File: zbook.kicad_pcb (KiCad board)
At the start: 4 copper layers, 189 parts, among them J1 USB_C_Receptacle_USB2.0_16P, J2 B2B-XH-A, J3 USB_C_Receptacle_USB2.0_16P, J4 Conn_01x03_Pin, J5 Conn_01x05_Pin, J6 Conn_02x04_Odd_Even, J7 Conn_02x15_Counter_Clockwise, J8 MSD-4-A, J9 DISPLAY CONN, Q1 Q_NMOS_GSD, Q2 Q_Photo_NPN, Q3 SL2301S, Q4 T2N7002AK,LM, SW1 SW_SPDT, SW2 SW_Push, SW3 SW_Push, SW4 SW_Push, SW5 SW_Push, SW6 SW_Push, SW7 SW_Push, U3 RP2040, U5 W25Q16JVSS, U6 W25Q16JVSS, U7 GSDA213, Y1 12MHz/10pF, Y2 12MHz/10pF

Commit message: wip: placement
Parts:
- added Q5: T2N7002AK,LM, Package_TO_SOT_SMD:SOT-23, F.Cu at (134.3, 97.3)
- added R56: 10k, Resistor_SMD:R_0402_1005Metric, F.Cu at (136.8, 97.3)
- J4: value Conn_01x03_Pin -> Conn_01x05_Pin; footprint Connector_PinHeader_2.54mm:PinHeader_1x03_P2.54mm_Vertical -> microcontroller:PogoPins
- moved FID1 357.5 mm to (59.6, 75.2)
- moved FID3 353.9 mm to (62.8, 88.2)
- moved H1 350.8 mm to (61.2, 81.2)
- moved H3 349.3 mm to (64.4, 75.6)
- moved FID4 348.8 mm to (68.8, 79.1)
- moved FID2 344.2 mm to (72.8, 81.0)
- moved H2 344.1 mm to (68.0, 86.4)
- moved H4 340.7 mm to (73.9, 75.8)
- moved R24 333.1 mm to (75.3, 83.2)
- moved R55 323.7 mm to (81.5, 136.0), turned to 180 degrees
- moved R54 323.0 mm to (81.5, 132.7), turned to 180 degrees
- moved D8 321.8 mm to (69.3, 71.2)
- moved J6 318.1 mm to (84.7, 138.0), turned to 180 degrees
- moved C47 315.2 mm to (45.3, 77.3)
- moved C48 315.2 mm to (45.3, 79.3)
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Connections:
- BZ1 pad 1: Net-(BZ1-+) -> +3V3
- BZ1 pad 2: GND -> Net-(BZ1--)
- J4 pad 1: /Microcontroller/SWDIO_RP2040 -> +3V3
- J4 pad 3: GND -> /Microcontroller/SWDIO_RP2040
- J5 pad 1: /Microcontroller/RP2350_TX/BT_WIFI_RX -> /Microcontroller/RP2350_TX/BT_RX
- J5 pad 2: /Microcontroller/RP2350_RX/BT_WIFI_TX -> /Microcontroller/RP2350_RX/BT_TX
- J6 pad 2: /Microcontroller/RP2350_RX/BT_WIFI_TX -> /Microcontroller/RP2350_RX/BT_TX
- J6 pad 7: /Microcontroller/RP2350_TX/BT_WIFI_RX -> /Microcontroller/RP2350_TX/BT_RX
- J7 pad 1: /Microcontroller/GPIO06 -> /Microcontroller/GPIO07
- J7 pad 10: MOSFET_DRAIN -> I2C_SDA
- J7 pad 11: I2C_SDA -> I2C_SCL
- J7 pad 12: I2C_SCL -> SPI_MISO
- J7 pad 13: SPI_MISO -> SPI_SCLK
- J7 pad 14: SPI_SCLK -> SPI_MOSI
- J7 pad 15: SPI_MOSI -> /Microcontroller/RUN_RP2350
- J7 pad 2: /Microcontroller/GPIO07 -> /Microcontroller/GPIO08
- J7 pad 3: /Microcontroller/GPIO08 -> /Microcontroller/GPIO26
- J7 pad 4: /Microcontroller/GPIO26 -> /Microcontroller/GPIO27
- J7 pad 5: /Microcontroller/GPIO27 -> /Microcontroller/GPIO47
- J7 pad 6: /Microcontroller/GPIO47 -> /Microcontroller/GPIO46
- J7 pad 7: /Microcontroller/GPIO46 -> /Microcontroller/GPIO45
- J7 pad 9: /Microcontroller/GPIO45 -> MOSFET_DRAIN
- R35 pad 1: BUZZER_GPIO -> Net-(BZ1--)
- R35 pad 2: Net-(BZ1-+) -> +3V3
- U4 pad 3: /Microcontroller/GPIO06 -> LED_ADDR_GPIO
- U4 pad 9: DISPLAY_RST -> ~{DISPLAY_RST}
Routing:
- net /Power Supply/LDO_EN: track 0.00 -> 1.62 mm
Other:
- board text added: "+3V3"
- board text added: "+5V"
- board text added: "+VBQ"
- board text added: "B"
- board text added: "G"
- board text added: "IR"
- board text added: "R"
- board text added: "Y"

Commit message: feat: finishes first iteration of placement
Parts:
- moved C48 128.3 mm to (166.8, 120.4), turned to -90 degrees
- moved C47 128.1 mm to (165.9, 120.4), turned to -90 degrees
- moved R48 122.7 mm to (167.0, 117.2), turned to 90 degrees
- moved FID1 119.0 mm to (156.2, 144.6)
- moved H1 111.5 mm to (171.7, 66.6)
- moved H3 110.8 mm to (155.7, 138.3)
- moved FID3 108.8 mm to (170.2, 70.8)
- moved FID4 101.3 mm to (167.5, 101.8)
- moved TP13 100.2 mm to (134.5, 108.9)
- moved C50 97.8 mm to (138.9, 111.3), turned to 90 degrees
- moved C49 93.8 mm to (134.2, 111.3), turned to 90 degrees
- moved U7 92.1 mm to (136.6, 111.5)
- moved R46 89.9 mm to (133.8, 98.6), turned to 90 degrees
- moved R47 87.5 mm to (133.8, 100.4), turned to -90 degrees
- moved TP16 81.5 mm to (118.6, 105.5)
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
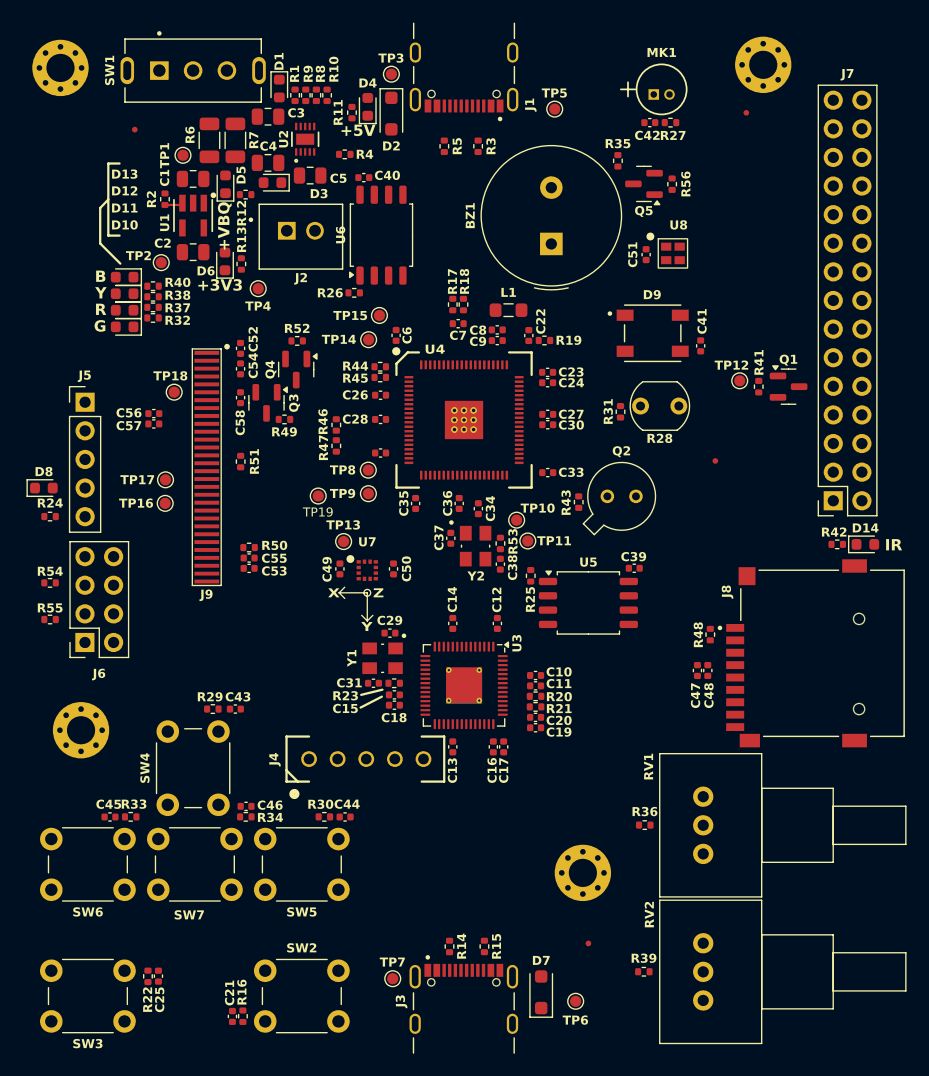
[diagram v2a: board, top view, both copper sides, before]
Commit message: feat: adds GND planes to L2 and L3
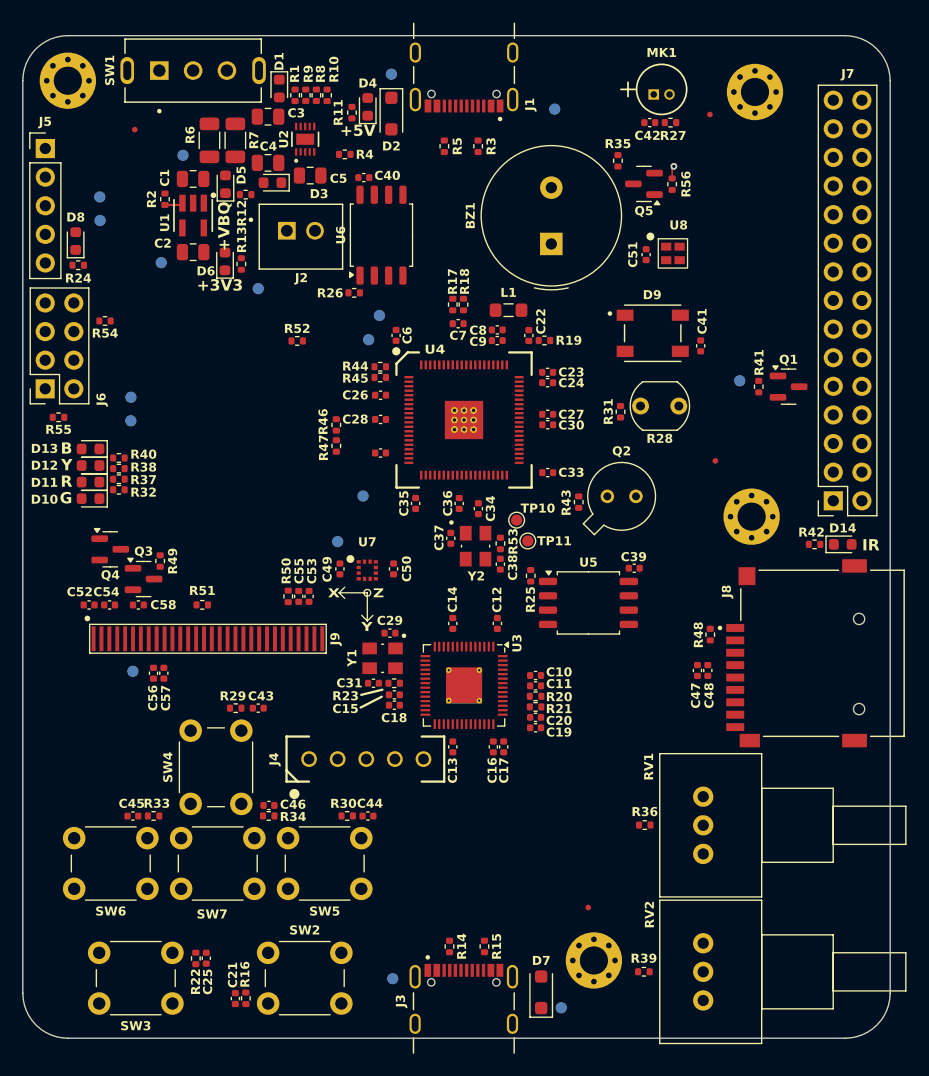
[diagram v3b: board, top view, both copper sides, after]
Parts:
- TP1, TP12, TP13, TP14, TP15, TP16, TP17, TP18, TP19, TP2, TP3, TP4, TP5, TP6, TP7, TP8, TP9: moved to B.Cu
- moved H2 62.5 mm to (170.7, 106.7)
- moved C52 26.5 mm to (111.9, 114.5), turned to 0 degrees
- moved TP17 25.8 mm to (112.8, 78.3), turned to 180 degrees
- moved TP16 25.8 mm to (112.9, 80.4), turned to 180 degrees
- moved TP18 25.0 mm to (115.8, 120.4), turned to -90 degrees
- moved C54 24.0 mm to (113.7, 114.5), turned to 0 degrees
- moved R54 23.8 mm to (113.3, 89.3), turned to 0 degrees
- moved C56 23.1 mm to (117.6, 120.6), turned to -90 degrees
- moved Q4 23.0 mm to (113.8, 109.6), turned to 0 degrees
- moved J5 22.8 mm to (108.0, 74.0)
- moved J6 22.8 mm to (108.0, 95.3)
- moved R24 22.4 mm to (110.9, 84.4), turned to 180 degrees
- moved C57 22.1 mm to (118.5, 120.6), turned to -90 degrees
- moved D8 22.1 mm to (110.7, 82.2), turned to 90 degrees
- moved TP9 22.1 mm to (115.6, 98.2), turned to 180 degrees
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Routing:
- net GND: track 0.00 -> 1.14 mm, vias 0 -> 1
- added copper zone on In1.Cu, net GND
- added copper zone on In2.Cu, net GND
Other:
- board outline added: 77 x 89 mm

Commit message: feat: starts routing
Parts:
- TP10, TP11: moved to B.Cu
- moved Q2 36.4 mm to (154.7, 68.6)
- moved R43 36.4 mm to (152.1, 69.1)
- moved J6 33.7 mm to (108.1, 129.0)
- moved R54 33.7 mm to (113.4, 123.0)
- moved R55 33.7 mm to (109.3, 131.5)
- moved TP16 29.5 mm to (132.8, 102.2)
- moved TP17 29.0 mm to (131.5, 100.5)
- moved R52 26.6 mm to (111.2, 109.6), turned to -90 degrees
- moved D10 25.9 mm to (115.1, 79.4), turned to 90 degrees
- moved D11 24.2 mm to (112.2, 79.4), turned to 90 degrees
- moved TP19 23.5 mm to (112.8, 106.6)
- moved D12 22.8 mm to (113.7, 79.4), turned to 90 degrees
- moved R32 22.4 mm to (114.9, 81.9), turned to 90 degrees
- moved D13 21.8 mm to (116.6, 79.4), turned to 90 degrees
- moved R37 21.5 mm to (113.0, 81.9), turned to 90 degrees
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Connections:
- C10 pad 1: +1V1 -> +1V1_PROBE
- C18 pad 1: +1V1 -> +1V1_PROBE
- C20 pad 2: +1V1 -> +1V1_PROBE
- U3 pad 23: +1V1 -> +1V1_PROBE
- U3 pad 45: +1V1 -> +1V1_PROBE
- U3 pad 50: +1V1 -> +1V1_PROBE
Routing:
- net +3V3: track 0.00 -> 160.8 mm, vias 0 -> 45
- net GND: track 1.14 -> 106.0 mm, vias 1 -> 123
- net /Microcontroller/RUN_RP2350: track 0.00 -> 72.0 mm, vias 0 -> 3
- net /Microcontroller/RUN_RP2040: track 0.00 -> 47.1 mm
- net SPI_SCLK: track 0.00 -> 43.9 mm, vias 0 -> 5
- net +VBUS: track 0.00 -> 43.9 mm, vias 0 -> 4
- net SD_DAT1: track 0.00 -> 40.9 mm, vias 0 -> 2
- net SPI_MOSI: track 0.00 -> 40.8 mm, vias 0 -> 1
- net SD_CD/DAT3: track 0.00 -> 37.5 mm
- net SD_DAT0: track 0.00 -> 37.3 mm, vias 0 -> 2
- net ~{SPI_DISPLAY_CS}: track 0.00 -> 36.4 mm
- net DISPLAY_EN: track 0.00 -> 35.9 mm
- net ~{LED_RED_GPIO}: track 0.00 -> 35.4 mm
- net ~{LED_YELLOW_GPIO}: track 0.00 -> 34.6 mm
- net SD_CLK: track 0.00 -> 34.5 mm
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- added copper zone on F.Cu, net +1V1
- added copper zone on B.Cu, net +3V3
- added copper zone on F.Cu, net +3V3
- added copper zone on F.Cu, net +BATT
- added copper zone on F.Cu, net +VBQ
- added copper zone on B.Cu, net +VBUS
- added copper zone on F.Cu, net +VBUS
- added copper zone on F.Cu, net GND
- added copper zone on B.Cu, net Net-(D2-A)
- added copper zone on F.Cu, net Net-(D2-A)
- added copper zone on B.Cu, net Net-(D7-A)
- added copper zone on F.Cu, net Net-(D7-A)

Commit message: wip: adds more routing
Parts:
- removed the C25 at (122.3, 145.9)
- removed the C3 at (127.8, 71.2)
- removed the C4 at (127.8, 75.3)
- removed the C5 at (131.5, 76.4)
- removed the D1 at (130.1, 66.6)
- removed the D3 at (128.2, 77.0)
- removed the D5 at (124.0, 77.2)
- removed the J2 at (130.7, 81.8)
- removed the R1 at (130.2, 69.3)
- removed the R10 at (133.0, 69.3)
- removed the R12 at (125.8, 78.1)
- removed the R2 at (118.6, 78.5)
- removed the R22 at (121.4, 145.9)
- removed the R39 at (161.1, 134.1)
- removed the R4 at (134.6, 74.5)
- removed the R6 at (122.6, 73.3)
- removed the R7 at (124.9, 73.3)
- removed the R8 at (132.1, 69.3)
- removed the R9 at (131.1, 69.3)
- removed RV2: R_Pot_US, Potentiometer_THT:Potentiometer_Vishay_148-149_Single_Horizontal
- removed the SW1 at (121.1, 67.1)
- removed the SW3 at (119.3, 149.9)
- removed the TP4 at (129.5, 83.3)
- removed the U2 at (131.1, 73.2)
- D6: renamed from D9; value WS2812B -> FZ2812-5050
- moved R15 45.7 mm to (117.2, 77.4)
- moved J5 44.9 mm to (111.8, 84.3)
- moved R16 44.9 mm to (113.0, 86.8)
- moved SW1 41.3 mm to (168.9, 149.2), turned to 180 degrees
- moved C18 36.1 mm to (172.2, 145.2), turned to -90 degrees
- moved R7 34.2 mm to (171.3, 145.2), turned to -90 degrees
- moved C50 15.3 mm to (114.7, 129.8)
- moved C48 15.3 mm to (112.8, 129.8)
- moved R28 13.1 mm to (152.9, 86.8), turned to 180 degrees
- moved Q1 12.7 mm to (154.8, 88.2)
- moved R31 12.7 mm to (157.3, 88.2)
- moved R29 12.3 mm to (165.7, 135.7)
- moved RV1 12.3 mm to (170.9, 138.2)
- moved D5 10.1 mm to (108.7, 89.3), turned to 0 degrees
- moved C52 9.89 mm to (118.3, 130.5)
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- renumbered C13 to C10, C14 to C11, C15 to C12, C16 to C13, C17 to C14, C18 to C15, C19 to C16, C20 to C17, C21 to C18, C22 to C19, C23 to C20, C24 to C21, C26 to C22, C27 to C23, C28 to C24, C29 to C25, C30 to C26, C31 to C27, C32 to C28, C33 to C29, C6 to C3, C34 to C30, C35 to C31, C36 to C32, C37 to C33, C38 to C34, C39 to C35, C40 to C36, C41 to C37, C42 to C38, C43 to C39, C7 to C4, C44 to C40, C45 to C41, C46 to C42, C47 to C43, C48 to C44, C49 to C45, C50 to C46, C51 to C47, C52 to C48, C53 to C49, C8 to C5, C54 to C50, C55 to C51, C56 to C52, C57 to C53, C58 to C54, C9 to C6, C10 to C7, C11 to C8, C12 to C9, D2 to D1, D13 to D10, D14 to D11, D7 to D2, D4 to D3, D6 to D4, D8 to D5, D10 to D7, D11 to D8, D12 to D9, J3 to J2, J4 to J3, J5 to J4, J6 to J5, J7 to J6, J8 to J7, J9 to J8, Q5 to Q1, Q1 to Q2, Q2 to Q3, Q3 to Q4, Q4 to Q5, R3 to R1, R19 to R10, R20 to R11, R21 to R12, R24 to R13, R23 to R14, R54 to R15, R55 to R16, R53 to R17, R25 to R18, R26 to R19, R5 to R2, R27 to R20, R28 to R21, R29 to R22, R30 to R23, R31 to R24, R32 to R25, R33 to R26, R34 to R27, R35 to R28, R36 to R29, R14 to R3, R37 to R30, R56 to R31, R38 to R32, R40 to R33, R41 to R34, R42 to R35, R43 to R36, R44 to R37, R45 to R38, R46 to R39, R11 to R4, R47 to R40, R48 to R41, R49 to R42, R50 to R43, R51 to R44, R52 to R45, R13 to R5, R15 to R6, R16 to R7, R17 to R8, R18 to R9, SW2 to SW1, SW4 to SW2, SW5 to SW3, SW6 to SW4, SW7 to SW5, TP3 to TP1, TP11 to TP10, TP12 to TP11, TP13 to TP12, TP14 to TP13, TP15 to TP14, TP16 to TP15, TP17 to TP16, TP18 to TP17, TP19 to TP18, TP1 to TP2, TP2 to TP3, TP5 to TP4, TP6 to TP5, TP7 to TP6, TP8 to TP7, TP9 to TP8, TP10 to TP9, U3 to U2, U4 to U3, U5 to U4, U6 to U5, U7 to U6, U8 to U7
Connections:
- C1 pad 1: +VBQ -> +VBUS
- TP2 pad 1: +VBQ -> +VBUS
- U1 pad 1: +VBQ -> +VBUS
- U1 pad 3: /Power Supply/LDO_EN -> +VBUS
- U3 pad 23: BUTTON2_GPIO -> BUTTON4_GPIO
- U3 pad 25: BUTTON3_GPIO -> BUTTON2_GPIO
- U3 pad 26: BUTTON4_GPIO -> BUTTON3_GPIO
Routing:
- net /Microcontroller/RP2350_TX/BT_RX: track 0.00 -> 57.0 mm, vias 0 -> 2
- net BUTTON3_GPIO: track 9.34 -> 63.5 mm, vias 0 -> 2
- net SPI_MOSI: track 40.8 -> 93.9 mm, vias 1 -> 3
- net /Microcontroller/RP2350_RX/BT_TX: track 0.00 -> 51.6 mm, vias 0 -> 3
- net POTENTIOMETER1_ADC: track 6.51 -> 55.3 mm, vias 1 -> 2
- net BUTTON4_GPIO: track 11.0 -> 59.5 mm
- net BUTTON2_GPIO: track 9.63 -> 57.8 mm
- net SPI_SCLK: track 43.9 -> 87.8 mm, vias 5 -> 4
- net BUTTON1_GPIO: track 10.6 -> 53.7 mm, vias 1 -> 0
- net I2C_SCL: track 5.52 -> 47.8 mm, vias 2 -> 3
- net /Microcontroller/WIFI_EN: track 0.00 -> 42.0 mm, vias 0 -> 3
- net /Microcontroller/WIFI_RST: track 0.00 -> 41.6 mm, vias 0 -> 3
- net I2C_SDA: track 6.49 -> 47.2 mm, vias 2 -> 3
- net SPI_MISO: track 7.06 -> 47.6 mm, vias 0 -> 3
- net IR_REC_GPIO: track 2.54 -> 38.4 mm, vias 0 -> 2
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- removed copper zone on F.Cu, net +BATT
- removed copper zone on F.Cu, net +VBQ
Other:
- board text removed: "+VBQ"

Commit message: feat: finishes p1 routing
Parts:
- added TP19: TestPoint_Small, TestPoint:TestPoint_Pad_D1.0mm, B.Cu at (148.6, 112.4)
- added TP20: TestPoint_Small, TestPoint:TestPoint_Pad_D1.0mm, B.Cu at (145.4, 116.6)
- added TP21: TestPoint_Small, TestPoint:TestPoint_Pad_D1.0mm, B.Cu at (153.9, 119.4)
- moved H2 67.8 mm to (110.0, 137.0)
- moved J6 35.6 mm to (180.5, 69.8), turned to 0 degrees
- moved TP2 8.25 mm to (131.9, 72.7)
- moved TP4 5.58 mm to (157.8, 73.7)
- moved FID4 5.28 mm to (167.5, 97.1)
- moved FID1 5.22 mm to (152.2, 138.1)
- moved R34 4.07 mm to (173.2, 98.8), turned to 0 degrees
- moved TP9 1.80 mm to (148.8, 110.2)
- moved C48 1.57 mm to (113.5, 131.2)
- moved C50 1.57 mm to (115.4, 131.2)
- moved C52 1.17 mm to (118.6, 131.6)
- moved C53 1.17 mm to (119.5, 131.6)
- moved H3 1.14 mm to (157.0, 145.0)
- moved Q2 1.01 mm to (173.6, 96.1), turned to 90 degrees
- moved TP11 0.93 mm to (169.3, 95.5)
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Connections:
- J6 pad 1: /Microcontroller/GPIO07 -> +3V3
- J6 pad 10: I2C_SDA -> /Microcontroller/GPIO07
- J6 pad 11: I2C_SCL -> GND
- J6 pad 12: SPI_MISO -> /Microcontroller/GPIO43
- J6 pad 13: SPI_SCLK -> GND
- J6 pad 14: SPI_MOSI -> /Microcontroller/GPIO47
- J6 pad 15: /Microcontroller/RUN_RP2350 -> GND
- J6 pad 16: /Microcontroller/SWCLK -> /Microcontroller/GPIO46
- J6 pad 17: /Microcontroller/SWDIO -> GND
- J6 pad 18: GND -> /Microcontroller/GPIO45
- J6 pad 2: /Microcontroller/GPIO08 -> +VBUS
- J6 pad 20: GND -> /Microcontroller/GPIO44
- J6 pad 22: GND -> MOSFET_DRAIN
- J6 pad 24: GND -> SPI_MISO
- J6 pad 25: GND -> /Microcontroller/GPIO27
- J6 pad 26: GND -> /Microcontroller/GPIO26
- J6 pad 28: GND -> SPI_SCLK
- J6 pad 29: +VBUS -> GND
- J6 pad 3: /Microcontroller/GPIO26 -> GND
- J6 pad 30: +3V3 -> SPI_MOSI
- J6 pad 4: /Microcontroller/GPIO27 -> I2C_SCL
- J6 pad 5: /Microcontroller/GPIO47 -> GND
- J6 pad 6: /Microcontroller/GPIO46 -> I2C_SDA
- J6 pad 7: /Microcontroller/GPIO45 -> GND
- J6 pad 8: /Microcontroller/GPIO45 -> /Microcontroller/GPIO08
- J6 pad 9: MOSFET_DRAIN -> GND
- U3 pad 52: POTENTIOMETER2_ADC -> /Microcontroller/GPIO43
- U3 pad 55: /Microcontroller/GPIO45 -> /Microcontroller/GPIO44
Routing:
- net /Microcontroller/GPIO08: track 1.33 -> 46.5 mm, vias 0 -> 2
- net /Microcontroller/GPIO07: track 2.93 -> 45.0 mm, vias 1 -> 2
- net /Microcontroller/GPIO43: track 0.00 -> 37.2 mm, vias 0 -> 2
- net /Microcontroller/GPIO47: track 0.00 -> 34.0 mm
- net /Microcontroller/GPIO46: track 0.00 -> 32.1 mm
- net /Microcontroller/GPIO45: track 0.00 -> 30.3 mm
- net /Microcontroller/GPIO44: track 0.00 -> 29.4 mm
- net SPI_MISO: track 47.6 -> 63.1 mm
- net /Microcontroller/GPIO27: track 28.8 -> 43.7 mm
- net /Microcontroller/GPIO26: track 27.3 -> 40.8 mm
- net SPI_SCLK: track 87.8 -> 100.7 mm
- net SPI_MOSI: track 93.9 -> 105.5 mm
- net +3V3: track 137.9 -> 147.2 mm, vias 43 -> 53
- net IR_REC_GPIO: track 38.4 -> 45.6 mm
- net I2C_SCL: track 47.8 -> 54.5 mm
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
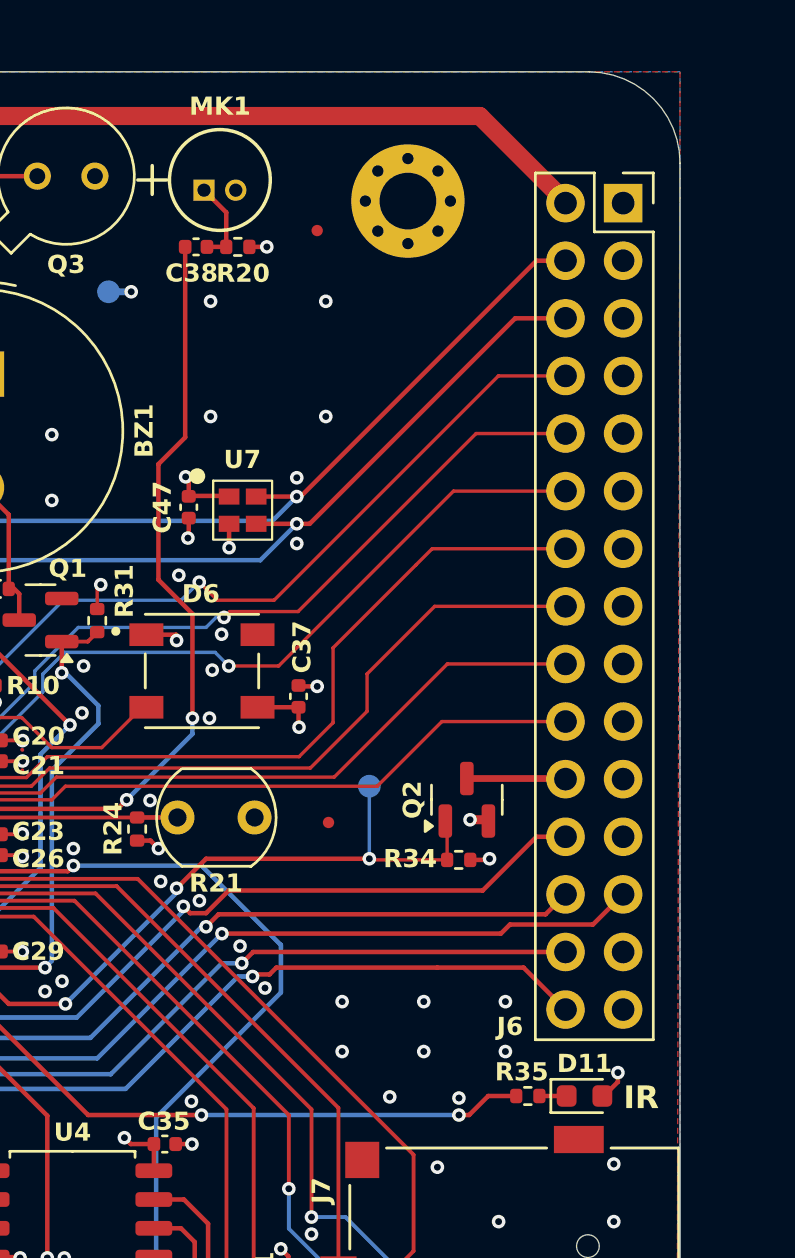
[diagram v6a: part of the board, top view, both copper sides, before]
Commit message: refac: changes IR emitter
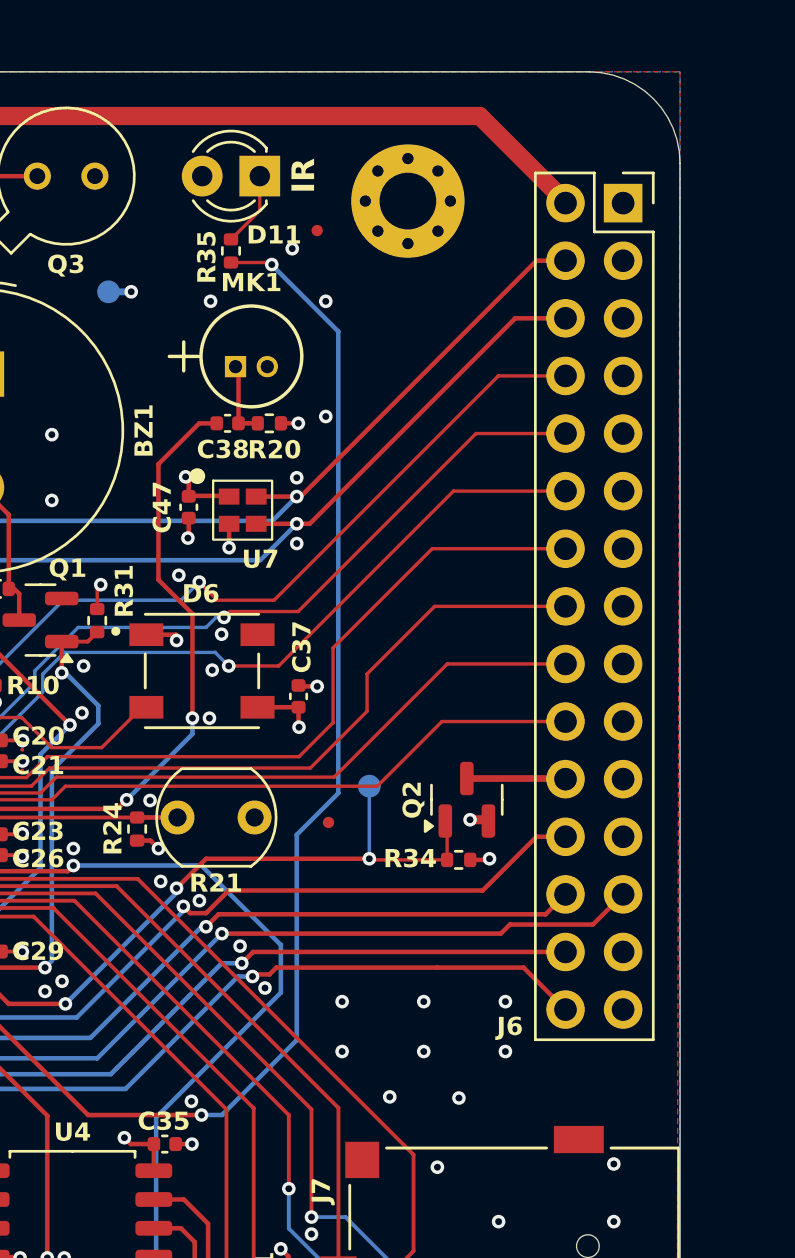
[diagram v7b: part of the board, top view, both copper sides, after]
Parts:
- D11: value IR204A -> INL-3AHIR15; footprint Diode_SMD:D_0603_1608Metric -> LED_THT:LED_D3.0mm_IRBlack
- moved D11 43.0 mm to (164.5, 68.6), turned to 180 degrees
- moved R35 39.5 mm to (163.2, 71.9), turned to 90 degrees
- moved C38 7.90 mm to (163.1, 79.5)
- moved MK1 7.90 mm to (163.4, 77.0)
- moved R20 7.90 mm to (164.9, 79.5)
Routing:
- net ~{IR_EMITTER_GPIO}: track 31.3 -> 60.6 mm
- net MICROPHONE_ADC: track 35.5 -> 28.7 mm
- net Net-(D11-K): track 1.20 -> 3.32 mm
- net +3V3: track 147.2 -> 145.8 mm, vias 53 -> 52
